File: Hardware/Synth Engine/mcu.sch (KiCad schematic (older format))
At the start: 27 parts, among them J3 SWD_programming, J7 Capsense_buttons, U6 CY8C4246AZI-L445, Y1 Crystal

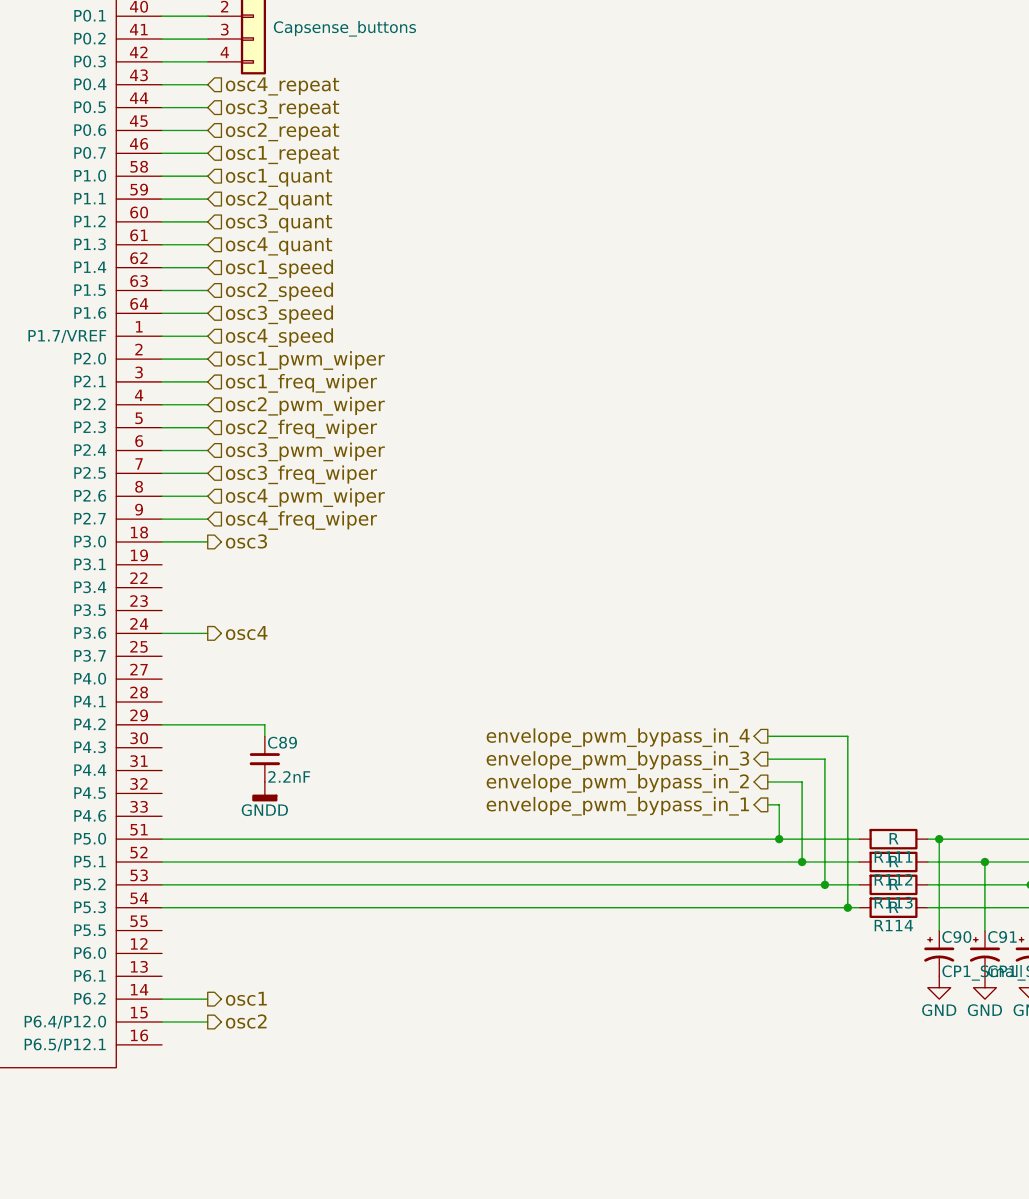
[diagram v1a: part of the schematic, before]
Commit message: redo connector routing with 2-row connectors
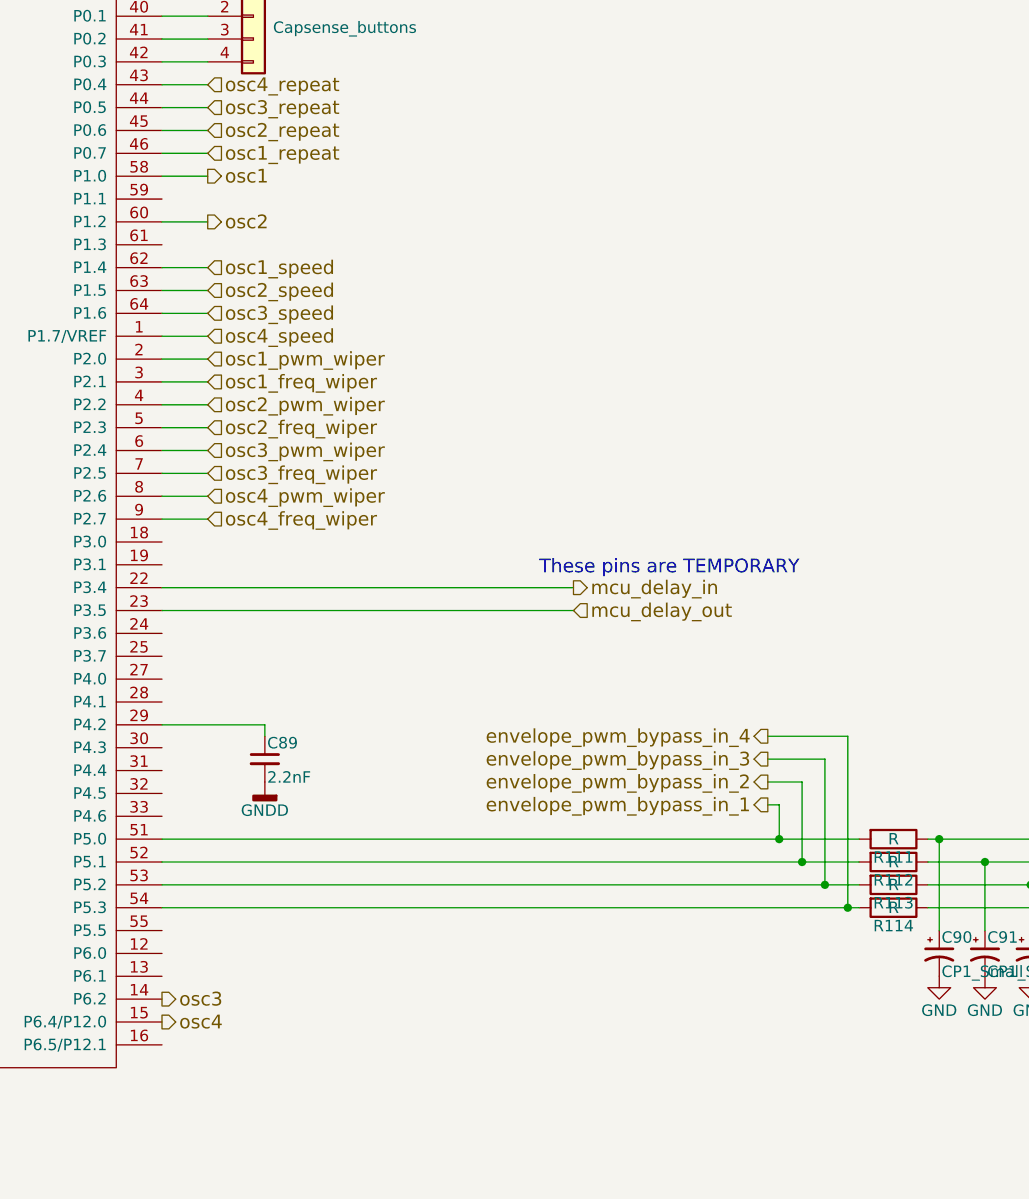
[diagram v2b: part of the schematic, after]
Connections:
- net osc1_quant is gone; now on net osc1: U6.58 (P1.0)
- net osc3_quant is gone; now on net osc2: U6.60 (P1.2)
- net osc1: no longer U6.14 (P6.2)
- net osc2: no longer U6.15 (P6.4/P12.0)
- net osc3: now also U6.14 (P6.2); no longer U6.18 (P3.0)
- net osc4: now also U6.15 (P6.4/P12.0); no longer U6.24 (P3.6)
- net mcu_delay_in: now reaches U6.22 (P3.4)
- net mcu_delay_out: now reaches U6.23 (P3.5)
- net osc2_quant: no longer names the net of U6.59 (P1.1)
- net osc4_quant: no longer names the net of U6.61 (P1.3)
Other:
- note added: "These pins are TEMPORARY"
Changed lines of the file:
@@
 $Descr A4 11693 8268
 encoding utf-8
-Sheet 7 8
+Sheet 6 8
 Title ""
 Date ""
@@
 Comment4 ""
 $EndDescr
-Text HLabel 5150 5600 2    60   Output ~ 0
+Text HLabel 5150 2000 2    60   Output ~ 0
 osc1
-Text HLabel 5150 5700 2    60   Output ~ 0
+Text HLabel 5150 2200 2    60   Output ~ 0
 osc2
-Text HLabel 5150 3600 2    60   Output ~ 0
+Text HLabel 4950 5600 2    60   Output ~ 0
 osc3
-Text HLabel 5150 4000 2    60   Output ~ 0
+Text HLabel 4950 5700 2    60   Output ~ 0
 osc4
 $Comp
@@
 $EndComp
 $Comp
-L GNDD #PWR085
+L GNDD #PWR92
 U 1 1 5C36CA45
 P 1300 7150
-F 0 "#PWR085" H 1300 6900 50  0001 C CNN
+F 0 "#PWR92" H 1300 6900 50  0001 C CNN
 F 1 "GNDD" H 1300 7025 50  0000 C CNN
 F 2 "" H 1300 7150 50  0001 C CNN
@@
 $EndComp
 $Comp
-L GNDD #PWR086
+L GNDD #PWR93
 U 1 1 5C36DE0D
 P 1500 5050
-F 0 "#PWR086" H 1500 4800 50  0001 C CNN
+F 0 "#PWR93" H 1500 4800 50  0001 C CNN
 F 1 "GNDD" H 1500 4925 50  0000 C CNN
 F 2 "" H 1500 5050 50  0001 C CNN
@@
 $EndComp
 $Comp
-L GNDD #PWR087
+L GNDD #PWR98
 U 1 1 5C36DE61
 P 2000 5050
-F 0 "#PWR087" H 2000 4800 50  0001 C CNN
+F 0 "#PWR98" H 2000 4800 50  0001 C CNN
 F 1 "GNDD" H 2000 4925 50  0000 C CNN
 F 2 "" H 2000 5050 50  0001 C CNN
@@
 envelope_pwm_4
 $Comp
-L GNDD #PWR088
+L GNDD #PWR95
 U 1 1 5C3F1075
 P 1800 3250
-F 0 "#PWR088" H 1800 3000 50  0001 C CNN
+F 0 "#PWR95" H 1800 3000 50  0001 C CNN
 F 1 "GNDD" H 1800 3125 50  0000 C CNN
 F 2 "" H 1800 3250 50  0001 C CNN
@@
 $EndComp
 $Comp
-L GNDD #PWR089
+L GNDD #PWR85
 U 1 1 5C3F13C8
 P 750 6300
-F 0 "#PWR089" H 750 6050 50  0001 C CNN
+F 0 "#PWR85" H 750 6050 50  0001 C CNN
 F 1 "GNDD" H 750 6175 50  0000 C CNN
 F 2 "" H 750 6300 50  0001 C CNN
@@
 $EndComp
 $Comp
-L GND #PWR090
+L GND #PWR86
 U 1 1 5C3F1411
 P 1050 6300
-F 0 "#PWR090" H 1050 6050 50  0001 C CNN
+F 0 "#PWR86" H 1050 6050 50  0001 C CNN
 F 1 "GND" H 1050 6150 50  0000 C CNN
 F 2 "" H 1050 6300 50  0001 C CNN
@@
 $EndComp
 $Comp
-L GNDD #PWR091
+L GNDD #PWR100
 U 1 1 5C3FBFC0
 P 2100 4200
-F 0 "#PWR091" H 2100 3950 50  0001 C CNN
+F 0 "#PWR100" H 2100 3950 50  0001 C CNN
 F 1 "GNDD" H 2100 4075 50  0000 C CNN
 F 2 "" H 2100 4200 50  0001 C CNN
@@
 $EndComp
 $Comp
-L GNDD #PWR092
+L GNDD #PWR90
 U 1 1 5C3FE25C
 P 1150 3950
-F 0 "#PWR092" H 1150 3700 50  0001 C CNN
+F 0 "#PWR90" H 1150 3700 50  0001 C CNN
 F 1 "GNDD" H 1150 3825 50  0000 C CNN
 F 2 "" H 1150 3950 50  0001 C CNN
@@
 $EndComp
 $Comp
-L GNDD #PWR093
+L GNDD #PWR88
 U 1 1 5C3FE41C
 P 1150 3400
-F 0 "#PWR093" H 1150 3150 50  0001 C CNN
+F 0 "#PWR88" H 1150 3150 50  0001 C CNN
 F 1 "GNDD" H 1150 3275 50  0000 C CNN
 F 2 "" H 1150 3400 50  0001 C CNN
@@
 $EndComp
 $Comp
-L GNDD #PWR094
+L GNDD #PWR96
 U 1 1 5C3FE65E
 P 1800 3900
-F 0 "#PWR094" H 1800 3650 50  0001 C CNN
+F 0 "#PWR96" H 1800 3650 50  0001 C CNN
 F 1 "GNDD" H 1800 3775 50  0000 C CNN
 F 2 "" H 1800 3900 50  0001 C CNN
@@
 $EndComp
 $Comp
-L GNDD #PWR095
+L GNDD #PWR101
 U 1 1 5C534CC8
 P 5400 4650
-F 0 "#PWR095" H 5400 4400 50  0001 C CNN
+F 0 "#PWR101" H 5400 4400 50  0001 C CNN
 F 1 "GNDD" H 5400 4525 50  0000 C CNN
 F 2 "" H 5400 4650 50  0001 C CNN
@@
 $EndComp
 $Comp
-L +5V #PWR096
+L +5V #PWR99
 U 1 1 5C548F91
 P 2050 1700
-F 0 "#PWR096" H 2050 1550 50  0001 C CNN
+F 0 "#PWR99" H 2050 1550 50  0001 C CNN
 F 1 "+5V" H 2050 1840 50  0000 C CNN
 F 2 "" H 2050 1700 50  0001 C CNN
@@
 $EndComp
 $Comp
-L +5V #PWR097
+L +5V #PWR87
 U 1 1 5C549089
 P 1150 3200
-F 0 "#PWR097" H 1150 3050 50  0001 C CNN
+F 0 "#PWR87" H 1150 3050 50  0001 C CNN
 F 1 "+5V" H 1150 3340 50  0000 C CNN
 F 2 "" H 1150 3200 50  0001 C CNN
@@
 $EndComp
 $Comp
-L +5V #PWR098
+L +5V #PWR94
 U 1 1 5C549378
 P 1800 3050
-F 0 "#PWR098" H 1800 2900 50  0001 C CNN
+F 0 "#PWR94" H 1800 2900 50  0001 C CNN
 F 1 "+5V" H 1800 3190 50  0000 C CNN
 F 2 "" H 1800 3050 50  0001 C CNN
@@
 $EndComp
 $Comp
-L +5V #PWR099
+L +5V #PWR89
 U 1 1 5C54940D
 P 1150 3750
-F 0 "#PWR099" H 1150 3600 50  0001 C CNN
+F 0 "#PWR89" H 1150 3600 50  0001 C CNN
 F 1 "+5V" H 1150 3890 50  0000 C CNN
 F 2 "" H 1150 3750 50  0001 C CNN
@@
 $EndComp
 $Comp
-L +5V #PWR0100
+L +5V #PWR97
 U 1 1 5C5494A2
 P 1800 4100
-F 0 "#PWR0100" H 1800 3950 50  0001 C CNN
+F 0 "#PWR97" H 1800 3950 50  0001 C CNN
 F 1 "+5V" H 1800 4240 50  0000 C CNN
 F 2 "" H 1800 4100 50  0001 C CNN
@@
 $EndComp
 $Comp
-L +5V #PWR0101
+L +5V #PWR91
 U 1 1 5C549537
 P 1300 7050
-F 0 "#PWR0101" H 1300 6900 50  0001 C CNN
+F 0 "#PWR91" H 1300 6900 50  0001 C CNN
 F 1 "+5V" H 1300 7190 50  0000 C CNN
 F 2 "" H 1300 7050 50  0001 C CNN
@@
 $EndComp
 $Comp
-L GND #PWR0102
+L GND #PWR102
 U 1 1 5C5518EB
 P 8350 5500
-F 0 "#PWR0102" H 8350 5250 50  0001 C CNN
+F 0 "#PWR102" H 8350 5250 50  0001 C CNN
 F 1 "GND" H 8350 5350 50  0000 C CNN
 F 2 "" H 8350 5500 50  0001 C CNN
@@
 $EndComp
 $Comp
-L GND #PWR0103
+L GND #PWR103
 U 1 1 5C551A2C
 P 8550 5500
-F 0 "#PWR0103" H 8550 5250 50  0001 C CNN
+F 0 "#PWR103" H 8550 5250 50  0001 C CNN
 F 1 "GND" H 8550 5350 50  0000 C CNN
 F 2 "" H 8550 5500 50  0001 C CNN
@@
 $EndComp
 $Comp
-L GND #PWR0104
+L GND #PWR104
 U 1 1 5C551AF1
 P 8750 5500
-F 0 "#PWR0104" H 8750 5250 50  0001 C CNN
+F 0 "#PWR104" H 8750 5250 50  0001 C CNN
 F 1 "GND" H 8750 5350 50  0000 C CNN
 F 2 "" H 8750 5500 50  0001 C CNN
@@
 $EndComp
 $Comp
-L GND #PWR0105
+L GND #PWR105
 U 1 1 5C551BB6
 P 8950 5500
-F 0 "#PWR0105" H 8950 5250 50  0001 C CNN
+F 0 "#PWR105" H 8950 5250 50  0001 C CNN
 F 1 "GND" H 8950 5350 50  0000 C CNN
 F 2 "" H 8950 5500 50  0001 C CNN
@@
 Text HLabel 5150 2700 2    60   Input ~ 0
 osc4_speed
-Text HLabel 5150 2000 2    60   Input ~ 0
-osc1_quant
-Text HLabel 5150 2100 2    60   Input ~ 0
-osc2_quant
-Text HLabel 5150 2200 2    60   Input ~ 0
-osc3_quant
-Text HLabel 5150 2300 2    60   Input ~ 0
-osc4_quant
 Text HLabel 5150 1900 2    60   Input ~ 0
 osc1_repeat
@@
 	5150 2600 4950 2600
 Wire Wire Line
-	5150 3600 4950 3600
-Wire Wire Line
-	5150 4000 4950 4000
-Wire Wire Line
-	5150 5600 4950 5600
-Wire Wire Line
-	4950 5700 5150 5700
-Wire Wire Line
 	4950 4900 8000 4900
 Wire Wire Line
@@
 	5150 2000 4950 2000
 Wire Wire Line
-	4950 2100 5150 2100
-Wire Wire Line
 	5150 2200 4950 2200
-Wire Wire Line
-	4950 2300 5150 2300
+Text HLabel 6750 3800 2    60   Output ~ 0
+mcu_delay_in
+Text HLabel 6750 3900 2    60   Input ~ 0
+mcu_delay_out
+Wire Wire Line
+	6750 3800 4950 3800
+Wire Wire Line
+	4950 3900 6750 3900
+Text Notes 6600 3750 0    60   ~ 0
+These pins are TEMPORARY
 $EndSCHEMATC

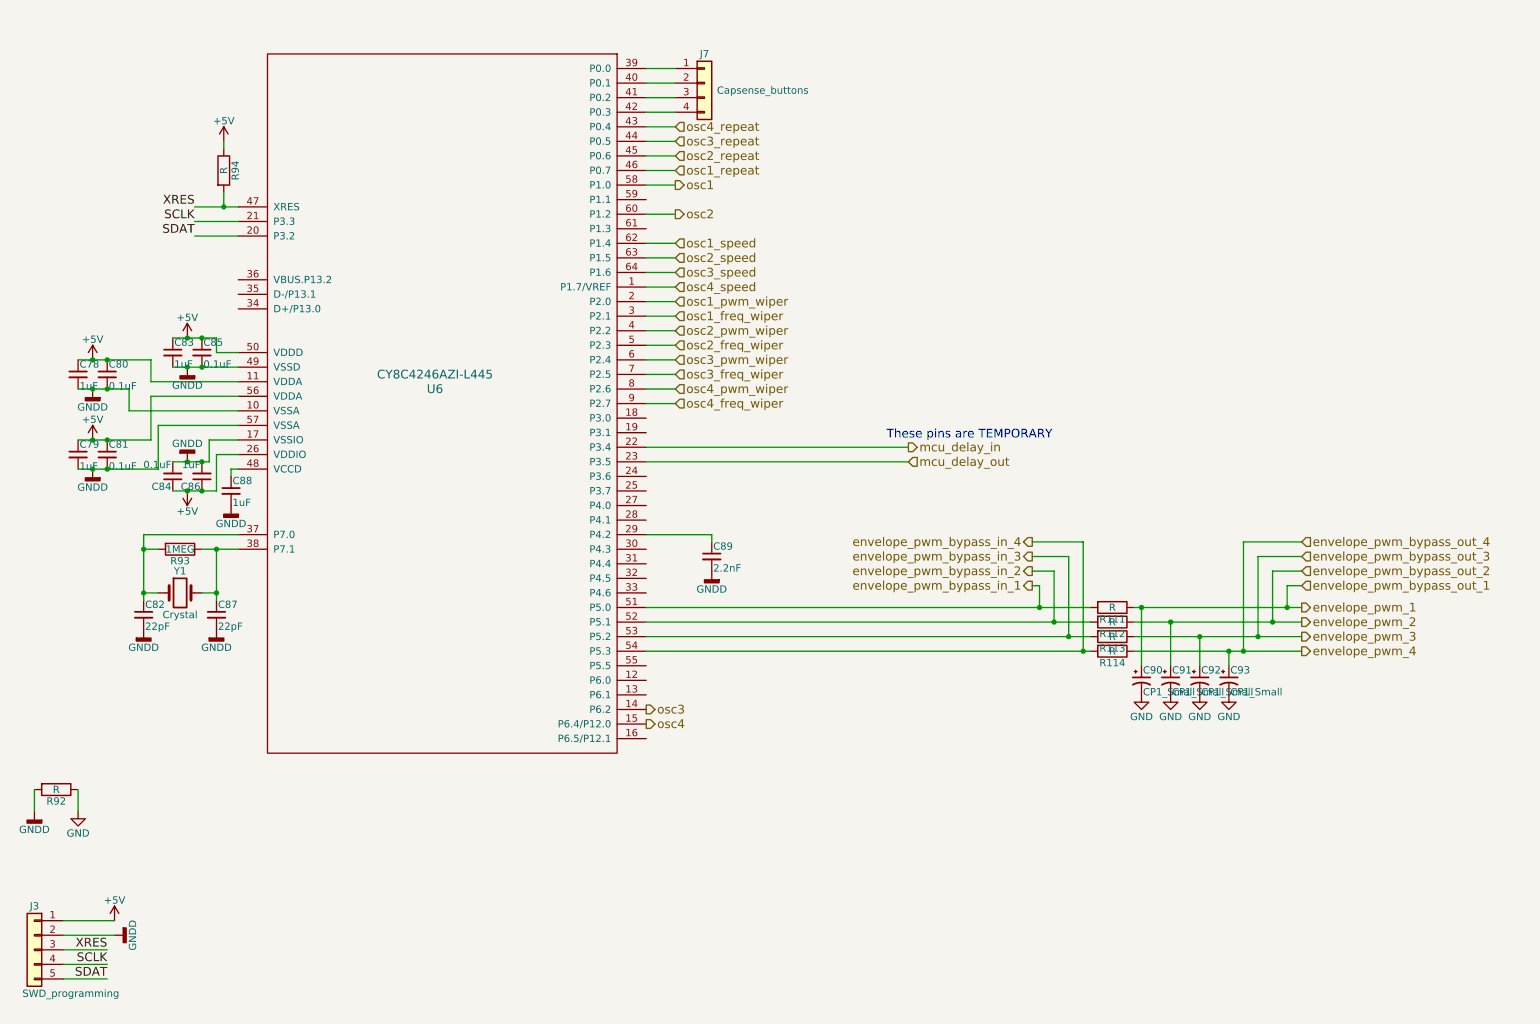
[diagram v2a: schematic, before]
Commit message: add quantization again, fix connectors again, add mounting holes to main board
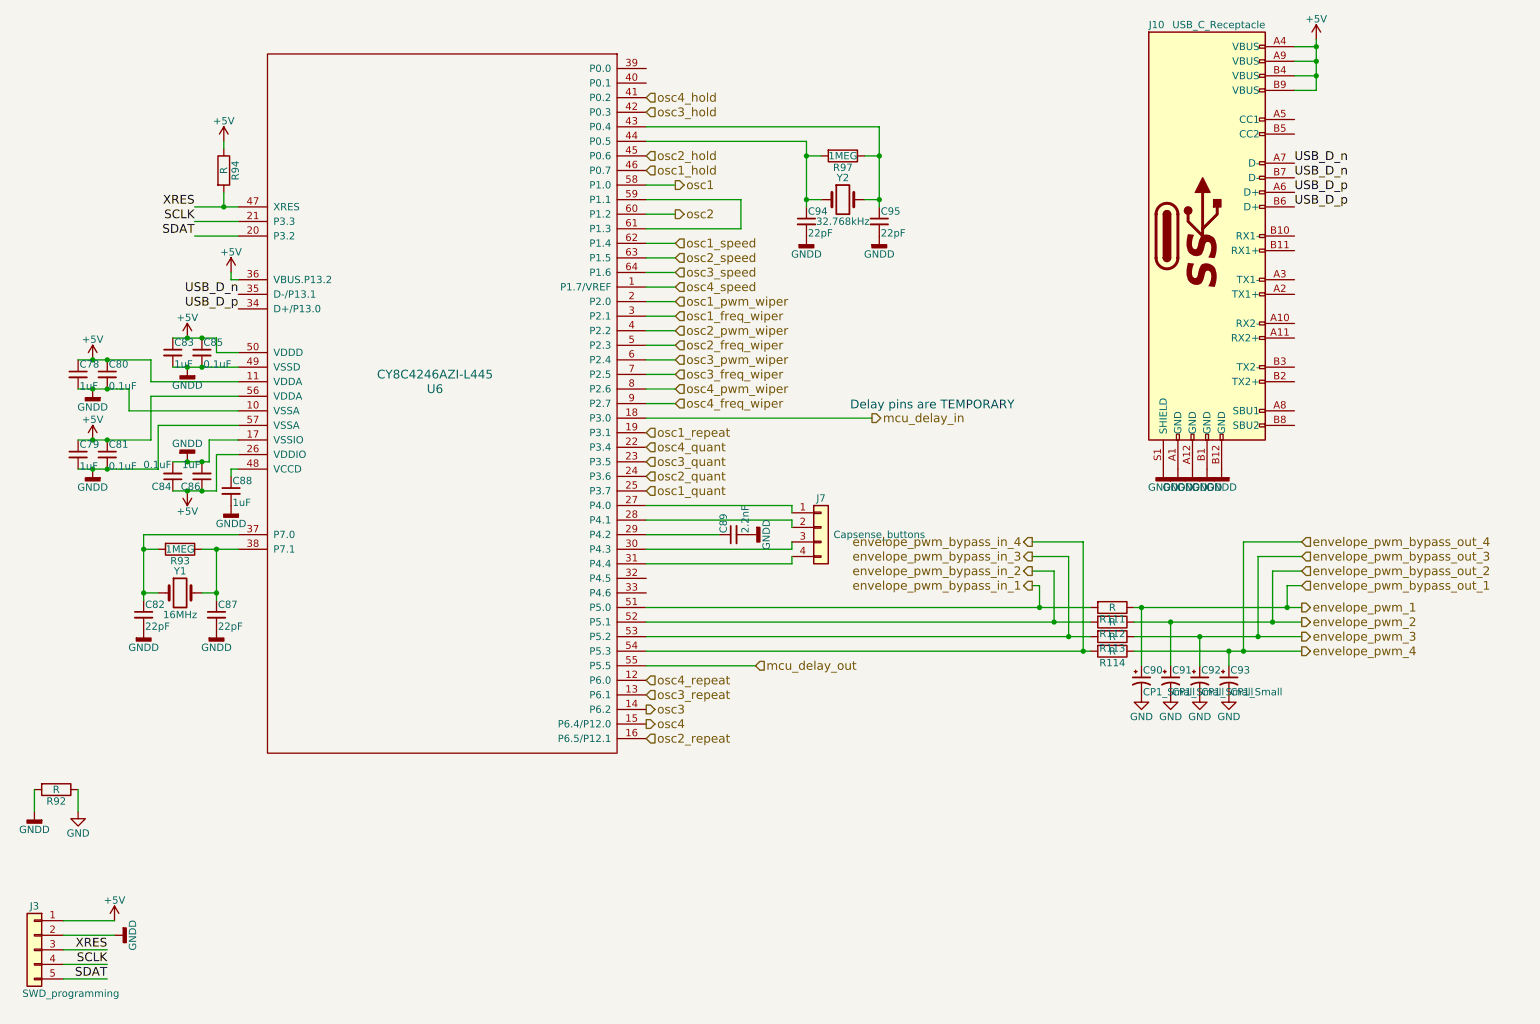
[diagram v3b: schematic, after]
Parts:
- added C94, C95: 22pF, digikey-footprints:0805, symbol C_Small
- added J10: USB_C_Receptacle, digikey-footprints:USB_Type_C_Female__12401610E4_2A, symbol USB_C_Receptacle
- added R97: 1MEG, digikey-footprints:0805, symbol R
- added Y2: 32.768kHz, digikey-footprints:1206, symbol Crystal
- Y1: value Crystal -> 16MHz
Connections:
- net +5V: now also U6.36 (VBUS.P13.2), J10.A4 (VBUS), J10.A9 (VBUS), J10.B4 (VBUS), J10.B9 (VBUS)
- net GNDD: now also C94.2, C95.2, J10.A1 (GND), J10.A12 (GND), J10.B1 (GND), J10.B12 (GND), J10.S1 (SHIELD)
- net mcu_delay_in: now also U6.18 (P3.0); no longer U6.22 (P3.4)
- net mcu_delay_out: now also U6.55 (P5.5); no longer U6.23 (P3.5)
- net osc1_repeat: now also U6.19 (P3.1); no longer U6.46 (P0.7)
- net osc2_repeat: now also U6.16 (P6.5/P12.1); no longer U6.45 (P0.6)
- net osc3_repeat: now also U6.13 (P6.1); no longer U6.44 (P0.5)
- net osc4_repeat: now also U6.12 (P6.0); no longer U6.43 (P0.4)
- net osc2_quant: now reaches U6.24 (P3.6)
- net osc1_quant: now reaches U6.25 (P3.7)
- net at U6.27 (P4.0): now also J7.1 (Pin_1)
- net at U6.28 (P4.1): now also J7.2 (Pin_2)
- net at U6.30 (P4.3): now also J7.3 (Pin_3)
- net at U6.31 (P4.4): now also J7.4 (Pin_4)
- net USB_D_p: now reaches U6.34 (D+/P13.0)
- net USB_D_p: now also J10.A6 (D+), J10.B6 (D+)
- net USB_D_n: now reaches U6.35 (D-/P13.1)
- net USB_D_n: now also J10.A7 (D-), J10.B7 (D-)
- net at U6.39 (P0.0): no longer J7.1 (Pin_1)
- net at U6.40 (P0.1): no longer J7.2 (Pin_2)
- net osc4_hold: now reaches U6.41 (P0.2)
- net osc4_hold: no longer J7.3 (Pin_3)
- net osc3_hold: now reaches U6.42 (P0.3)
- net osc3_hold: no longer J7.4 (Pin_4)
- net at U6.59 (P1.1): now also U6.61 (P1.3)
- new net: C95.1, R97.1, U6.43 (P0.4), Y2.2
- new net: C94.1, R97.2, U6.44 (P0.5), Y2.1
- new net osc1_hold: U6.46 (P0.7)
- new net osc2_hold: U6.45 (P0.6)
- new net osc3_quant: U6.23 (P3.5)
- new net osc4_quant: U6.22 (P3.4)
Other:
- note added: "Delay pins are TEMPORARY"
- note removed: "These pins are TEMPORARY"
- moved on the sheet: C89, J7
